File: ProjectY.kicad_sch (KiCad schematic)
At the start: 9 parts, among them J15 009155002852006, J16 009155002852006, J17 Out, J2 Conn_ARM_JTAG_SWD_10, J4 Conn_01x20, J5 IN_R, J6 IN_L, J7 Out, J9 USB_C_Receptacle_USB2.0_14P

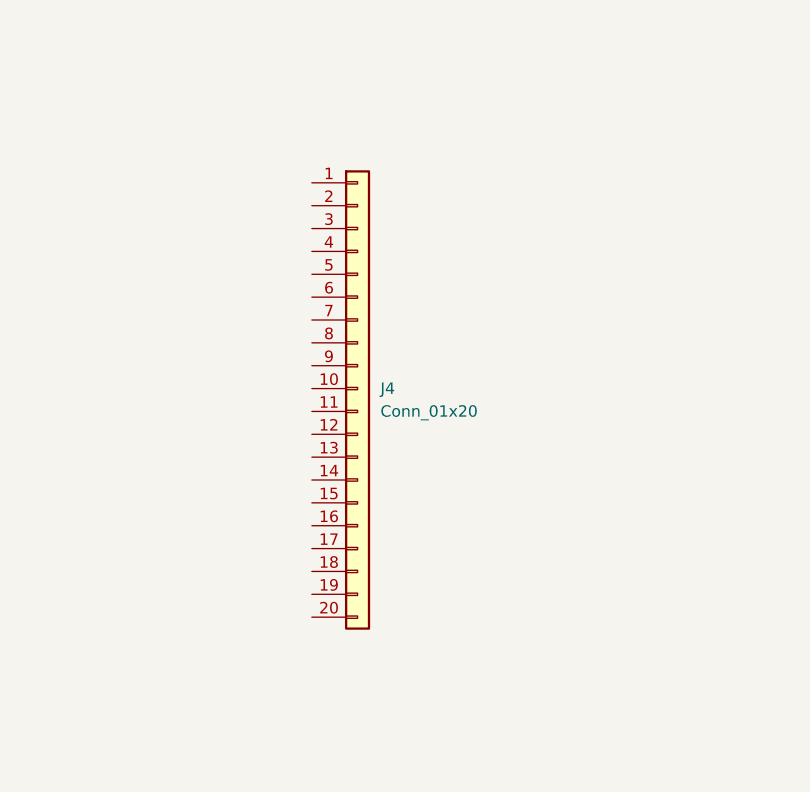
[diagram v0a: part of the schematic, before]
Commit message: added renesas RA8P1
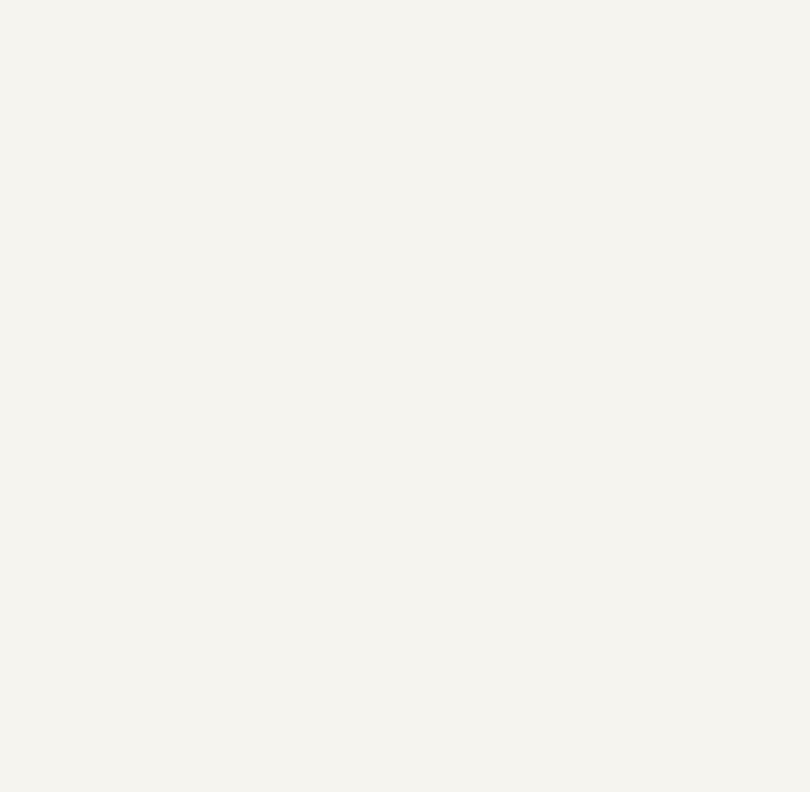
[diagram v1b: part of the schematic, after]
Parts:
- removed J4: Conn_01x20, symbol Connector_Generic:Conn_01x20
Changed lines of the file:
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@@
-	)
-	(symbol
-		(lib_id "Connector_Generic:Conn_01x20")
-		(at 110.49 104.14 0)
-		(unit 1)
-		(exclude_from_sim no)
-		(in_bom yes)
-		(on_board yes)
-		(dnp no)
-		(fields_autoplaced yes)
-		(property "Reference" "J4"
-			(at 113.03 104.1399 0)
-			(effects
-				(font
-					(size 1.27 1.27)
-				)
-				(justify left)
-			)
-		)
-		(property "Value" "Conn_01x20"
-			(at 113.03 106.6799 0)
-			(effects
-				(font
-					(size 1.27 1.27)
-				)
-				(justify left)
-			)
-		)
-		(property "Footprint" ""
-			(at 110.49 104.14 0)
-			(effects
-				(font
-					(size 1.27 1.27)
-				)
-				(hide yes)
-			)
-		)
-		(property "Datasheet" "~"
-			(at 110.49 104.14 0)
-			(effects
-				(font
-					(size 1.27 1.27)
-				)
-				(hide yes)
-			)
-		)
-		(property "Description" "Generic connector, single row, 01x20, script generated (kicad-library-utils/schlib/autogen/connector/)"
-			(at 110.49 104.14 0)
-			(effects
-				(font
-					(size 1.27 1.27)
-				)
-				(hide yes)
-			)
-		)
-		(pin "9"
-		)
-		(pin "4"
-		)
-		(pin "7"
-		)
-		(pin "20"
-		)
-		(pin "1"
-		)
-		(pin "8"
-		)
-		(pin "13"
-		)
-		(pin "11"
-		)
-		(pin "12"
-		)
-		(pin "14"
-		)
-		(pin "6"
-		)
-		(pin "5"
-		)
-		(pin "3"
-		)
-		(pin "2"
-		)
-		(pin "15"
-		)
-		(pin "10"
-		)
-		(pin "16"
-		)
-		(pin "17"
-		)
-		(pin "18"
-		)
-		(pin "19"
-		)
-		(instances
-			(project ""
-				(path "/6b669608-d244-47fa-b233-c11102b937f7"
-					(reference "J4")
-					(unit 1)
-				)
-			)
-		)
 	)
 	(symbol

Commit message: layout progress
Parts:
- removed J15, J16: 009155002852006, User:KYO_009155002852006, symbol Thunderscope_Rev5:CONN SPRING 2 PIN
- added H1, H2, H3: MountingHole, MountingHole:MountingHole_2.7mm_M2.5, symbol Mechanical:MountingHole
- J2: footprint (none) -> Connector_PinHeader_1.27mm:PinHeader_2x05_P1.27mm_Vertical_SMD
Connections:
- net Analog Audio/IN_L: now also J5.TN
- net GND: no longer J5.R, J5.RN, J5.S, J5.SN, J5.TN, J6.R, J6.RN, J6.S, J6.SN, J6.TN
- new net AGND: J5.R, J5.RN, J5.S, J5.SN, J6.R, J6.RN, J6.S, J6.SN, J6.TN
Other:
- removed sheet MIDI + UI
- sheet Analog Audio ports: added ~{Analog_Dry}; removed none
- sheet DSP ports: added ~{Analog_Dry}; removed Footswitch_1, Footswitch_2, Potentiometer_1, Potentiometer_2, Potentiometer_3, Potentiometer_4, Potentiometer_5, Potentiometer_6, Switch_1A, Switch_1B, Switch_2A, Switch_2B
- note removed: "Potentiometers Switches Footswitches LEDs"

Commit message: 0 airwires finally
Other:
- note added: "JLC06161H-3313A"
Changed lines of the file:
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@@
 		(comment 1 "Ákos Kovács")
+	)
+	(text "JLC06161H-3313A"
+		(exclude_from_sim no)
+		(at 34.036 231.902 0)
+		(effects
+			(font
+				(size 2.54 2.54)
+				(thickness 0.508)
+				(bold yes)
+			)
+		)
 	)
 	(junction
